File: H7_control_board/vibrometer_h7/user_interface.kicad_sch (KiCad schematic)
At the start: 14 parts, among them SW501 SW_Push

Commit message: working on getting ERC to run... almost there!
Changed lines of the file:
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@@
 					(size 1.27 1.27)
 				)
+				(hide yes)
 			)
 		)

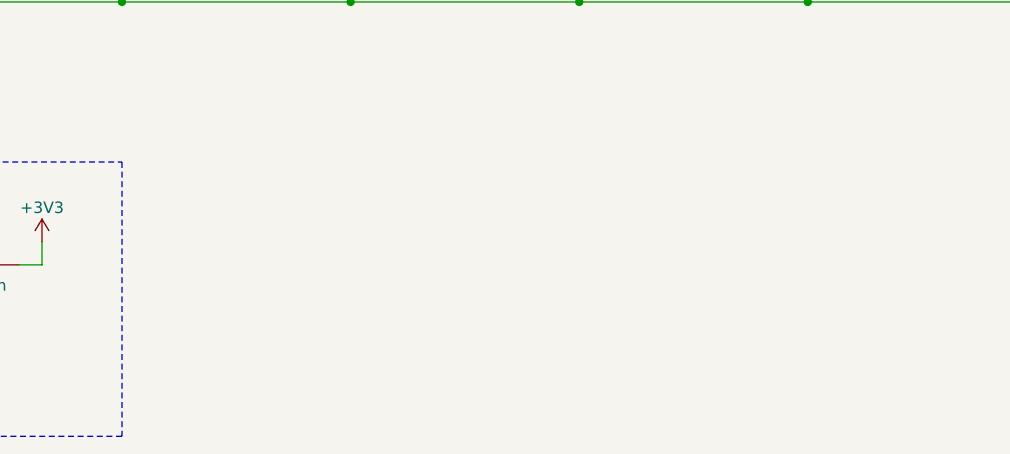
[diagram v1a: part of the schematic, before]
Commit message: adding strobe light to board itself
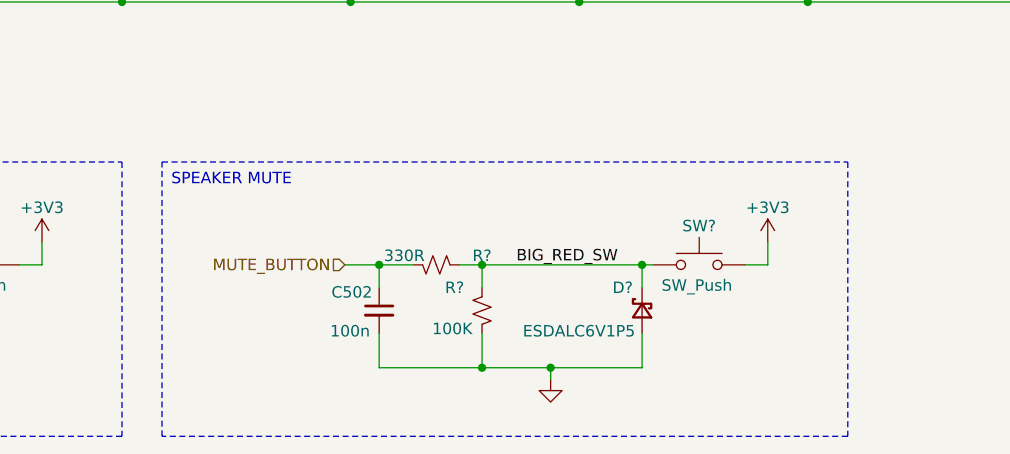
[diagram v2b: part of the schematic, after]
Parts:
- added C502: 100n, symbol Device:C_Small
- added D?: ESDALC6V1P5, symbol Device:D_Schottky_Small
- added R?: 100K, symbol Device:R_Small_US
- added R?: 330R, symbol Device:R_Small_US
- added SW?: SW_Push, symbol Switch:SW_Push
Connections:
- net +3V3: now also SW?.1
- net BIG_RED_SW: now also D?.1 (K), R?.1, R?.2, SW?.2
- net GND: now also C502.2, D?.2 (A), R?.1
- new net MUTE_BUTTON: C502.1, R?.2

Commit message: worked on audio output stuff, cleaned schematic
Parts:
- gave numbers to parts that had none: 3
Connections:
- net V_USB renamed +5V
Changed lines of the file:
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@@
+	)
+	(symbol
+		(lib_id "power:+5V")
+		(at 50.8 86.36 0)
+		(unit 1)
+		(exclude_from_sim no)
+		(in_bom yes)
+		(on_board yes)
+		(dnp no)
+		(property "Reference" "#PWR065"
+			(at 50.8 90.17 0)
+			(effects
+				(font
+					(size 1.27 1.27)
+				)
+				(hide yes)
+			)
+		)
+		(property "Value" "+5V"
+			(at 50.8 82.423 0)
+			(effects
+				(font
+					(size 1.27 1.27)
+				)
+			)
+		)
+		(property "Footprint" ""
+			(at 50.8 86.36 0)
+			(effects
+				(font
+					(size 1.27 1.27)
+				)
+				(hide yes)
+			)
+		)
+		(property "Datasheet" ""
+			(at 50.8 86.36 0)
+			(effects
+				(font
+					(size 1.27 1.27)
+				)
+				(hide yes)
+			)
+		)
+		(property "Description" "Power symbol creates a global label with name \"+5V\""
+			(at 50.8 86.36 0)
+			(effects
+				(font
+					(size 1.27 1.27)
+				)
+				(hide yes)
+			)
+		)
+		(pin "1"
+		)
+		(instances
+			(project "vibrometer_h7"
+				(path "/18de6987-156a-4b34-871e-cbbe1d261986/1264eea6-2da0-4b8c-9a4c-9121bcc9c76c"
+					(reference "#PWR065")
+					(unit 1)
+				)
+			)
+		)
 	)
 	(symbol
@@
 		(on_board yes)
 		(dnp no)
-		(property "Reference" "R?"
+		(property "Reference" "R504"
 			(at 163.957 140.97 0)
 			(effects
@@
 			(project "vibrometer_h7"
 				(path "/18de6987-156a-4b34-871e-cbbe1d261986/1264eea6-2da0-4b8c-9a4c-9121bcc9c76c"
-					(reference "R?")
-					(unit 1)
-				)
-			)
-		)
-	)
-	(symbol
-		(lib_id "power:+5V")
-		(at 50.8 86.36 0)
-		(unit 1)
-		(exclude_from_sim no)
-		(in_bom yes)
-		(on_board yes)
-		(dnp no)
-		(property "Reference" "#PWR065"
-			(at 50.8 90.17 0)
-			(effects
-				(font
-					(size 1.27 1.27)
-				)
-				(hide yes)
-			)
-		)
-		(property "Value" "V_USB"
-			(at 50.8 82.55 0)
-			(effects
-				(font
-					(size 1.27 1.27)
-				)
-			)
-		)
-		(property "Footprint" ""
-			(at 50.8 86.36 0)
-			(effects
-				(font
-					(size 1.27 1.27)
-				)
-				(hide yes)
-			)
-		)
-		(property "Datasheet" ""
-			(at 50.8 86.36 0)
-			(effects
-				(font
-					(size 1.27 1.27)
-				)
-				(hide yes)
-			)
-		)
-		(property "Description" "Power symbol creates a global label with name \"+5V\""
-			(at 50.8 86.36 0)
-			(effects
-				(font
-					(size 1.27 1.27)
-				)
-				(hide yes)
-			)
-		)
-		(pin "1"
-		)
-		(instances
-			(project "vibrometer_h7"
-				(path "/18de6987-156a-4b34-871e-cbbe1d261986/1264eea6-2da0-4b8c-9a4c-9121bcc9c76c"
-					(reference "#PWR065")
+					(reference "R504")
 					(unit 1)
 				)
@@
 		(on_board yes)
 		(dnp no)
-		(property "Reference" "D?"
+		(property "Reference" "D511"
 			(at 183.769 140.97 90)
 			(effects
@@
 			(project "vibrometer_h7"
 				(path "/18de6987-156a-4b34-871e-cbbe1d261986/1264eea6-2da0-4b8c-9a4c-9121bcc9c76c"
-					(reference "D?")
+					(reference "D511")
 					(unit 1)
 				)
@@
 		(on_board yes)
 		(dnp no)
-		(property "Reference" "R?"
+		(property "Reference" "R503"
 			(at 167.005 137.414 90)
 			(effects
@@
 			(project "vibrometer_h7"
 				(path "/18de6987-156a-4b34-871e-cbbe1d261986/1264eea6-2da0-4b8c-9a4c-9121bcc9c76c"
-					(reference "R?")
-					(unit 1)
-				)
+					(reference "R503")
+					(unit 1)
+				)

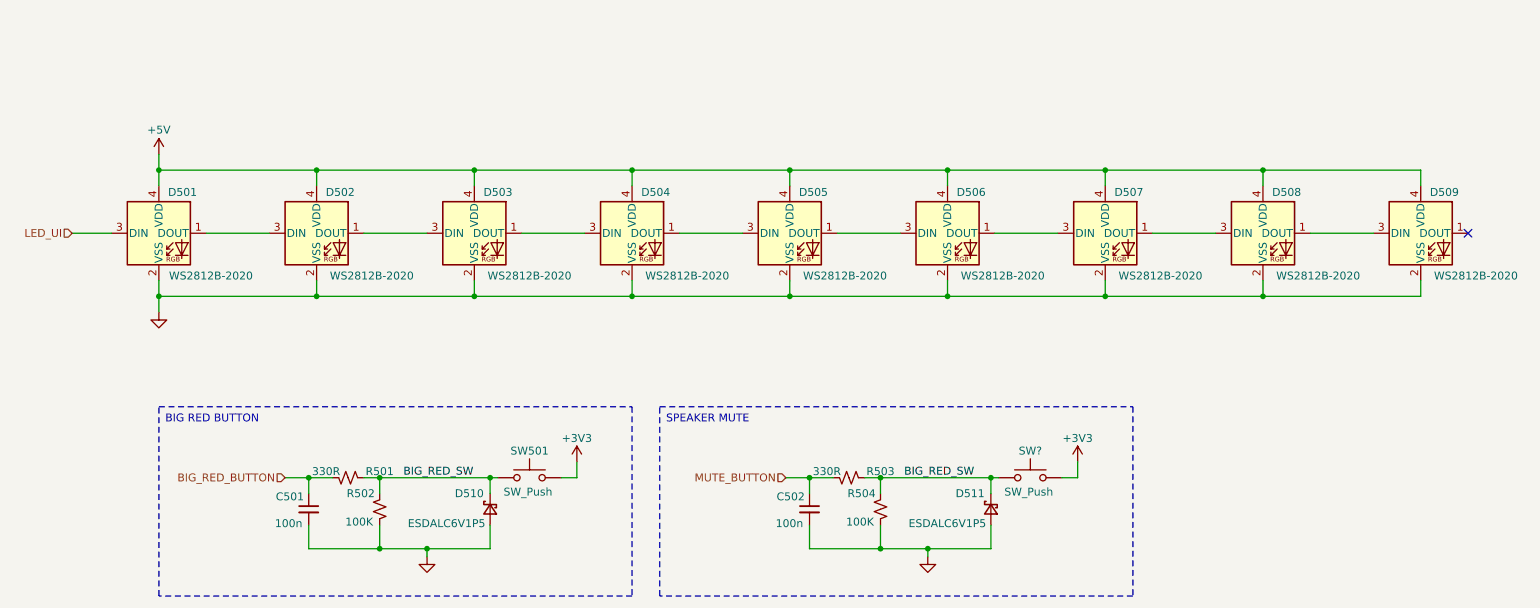
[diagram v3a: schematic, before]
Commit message: met with john to go over schematic. made changes, got rid of some leds...
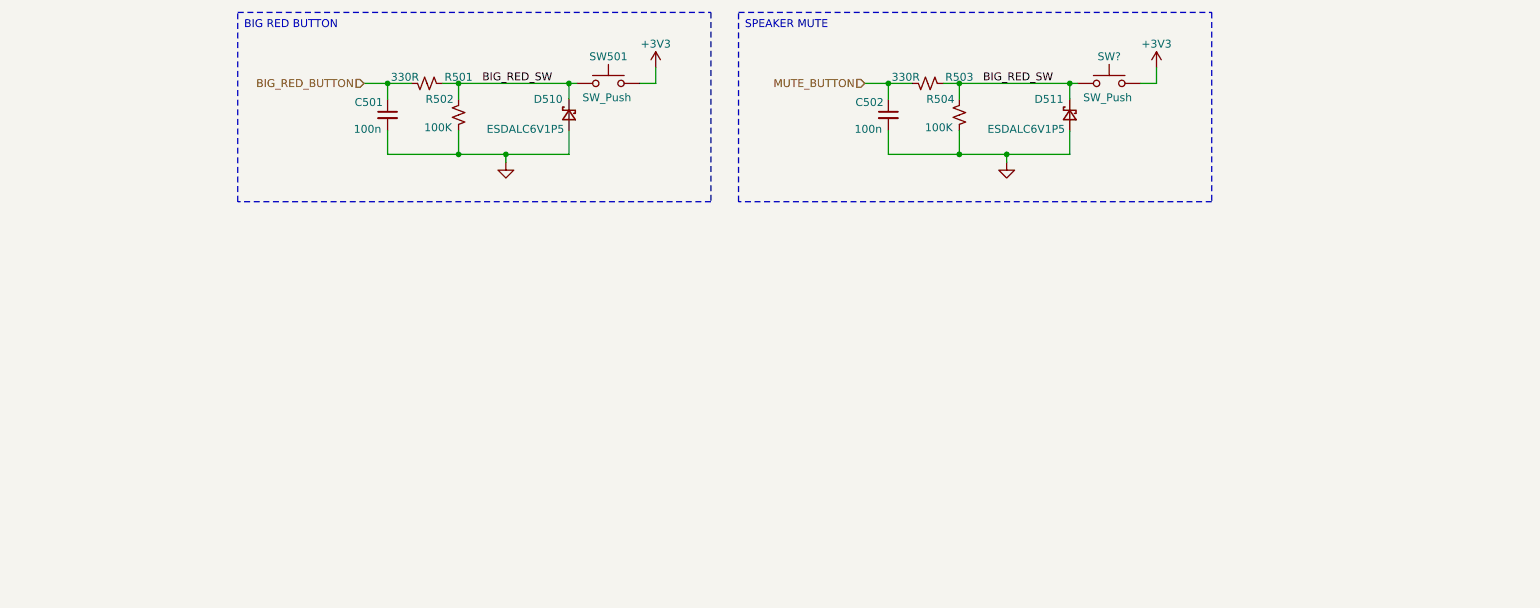
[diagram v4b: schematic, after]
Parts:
- removed D501, D502, D503, D504, D505, D506, D507, D508, D509: WS2812B-2020, LED_SMD:LED_WS2812B-2020_PLCC4_2.0x2.0mm, symbol LED:WS2812B-2020
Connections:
- no-connect marks 1 -> 0
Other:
- moved on the sheet: C501, C502, D510, D511, R501, R502, R503, R504, SW501, SW?

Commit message: started part selection
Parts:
- C501, C502: footprint (none) -> Capacitor_SMD:C_0603_1608Metric
- SW501, SW?: footprint (none) -> Button_Switch_SMD:SW_Push_1P1T_XKB_TS-1187A; LCSC (none) -> C318884
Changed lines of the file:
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@@
 			)
 		)
-		(property "Footprint" ""
+		(property "Footprint" "Capacitor_SMD:C_0603_1608Metric"
 			(at 168.275 80.01 0)
 			(effects
@@
 			)
 		)
-		(property "Footprint" ""
+		(property "Footprint" "Button_Switch_SMD:SW_Push_1P1T_XKB_TS-1187A"
 			(at 203.835 69.85 0)
 			(effects
@@
 			)
 		)
-		(property "Datasheet" "~"
+		(property "Datasheet" "https://www.lcsc.com/datasheet/lcsc_datasheet_2304140030_XKB-Connection-TS-1187A-B-A-B_C318884.pdf"
 			(at 203.835 69.85 0)
 			(effects
@@
 			)
 		)
-		(property "LCSC" ""
+		(property "LCSC" "C318884"
 			(at 203.835 74.93 0)
 			(effects
@@
 			)
 		)
-		(property "Footprint" ""
+		(property "Footprint" "Button_Switch_SMD:SW_Push_1P1T_XKB_TS-1187A"
 			(at 123.19 69.85 0)
 			(effects
@@
 			)
 		)
-		(property "Datasheet" "~"
+		(property "Datasheet" "https://www.lcsc.com/datasheet/lcsc_datasheet_2304140030_XKB-Connection-TS-1187A-B-A-B_C318884.pdf"
 			(at 123.19 69.85 0)
 			(effects
@@
 			)
 		)
-		(property "LCSC" ""
+		(property "LCSC" "C318884"
 			(at 123.19 74.93 0)
 			(effects
@@
 			)
 		)
-		(property "Footprint" ""
+		(property "Footprint" "Capacitor_SMD:C_0603_1608Metric"
 			(at 87.63 80.01 0)
 			(effects

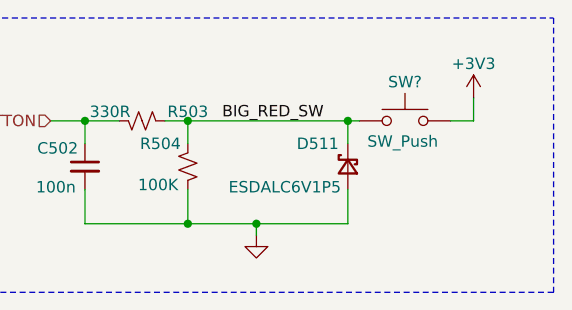
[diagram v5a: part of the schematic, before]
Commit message: component selection, headphone amp circuit specs
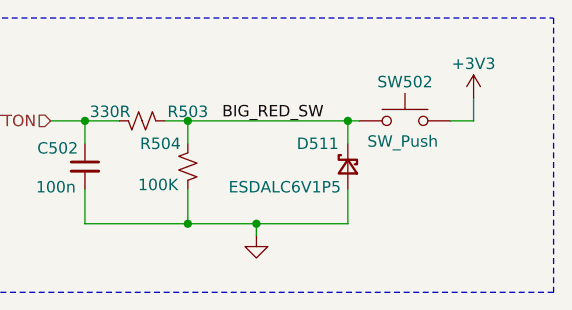
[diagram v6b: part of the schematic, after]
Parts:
- C501, C502: footprint Capacitor_SMD:C_0603_1608Metric -> Capacitor_SMD:C_0402_1005Metric_Pad0.74x0.62mm_HandSolder; LCSC (none) -> C307331
- gave numbers to parts that had none: 1
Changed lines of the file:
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@@
 			)
 		)
-		(property "Footprint" "Capacitor_SMD:C_0603_1608Metric"
+		(property "Footprint" "Capacitor_SMD:C_0402_1005Metric_Pad0.74x0.62mm_HandSolder"
 			(at 168.275 80.01 0)
 			(effects
@@
 			)
 		)
-		(property "Datasheet" "~"
+		(property "Datasheet" "https://wmsc.lcsc.com/wmsc/upload/file/pdf/v2/lcsc/2304140030_Samsung-Electro-Mechanics-CL05B104KB54PNC_C307331.pdf"
 			(at 168.275 80.01 0)
 			(effects
@@
 			)
 		)
-		(property "LCSC" ""
+		(property "LCSC" "C307331"
 			(at 168.275 80.01 0)
 			(effects
@@
 		(on_board yes)
 		(dnp no)
-		(property "Reference" "SW?"
+		(property "Reference" "SW502"
 			(at 203.835 70.612 0)
 			(effects
@@
 			(project "vibrometer_h7"
 				(path "/18de6987-156a-4b34-871e-cbbe1d261986/1264eea6-2da0-4b8c-9a4c-9121bcc9c76c"
-					(reference "SW?")
+					(reference "SW502")
 					(unit 1)
 				)
@@
 			)
 		)
-		(property "Footprint" "Capacitor_SMD:C_0603_1608Metric"
+		(property "Footprint" "Capacitor_SMD:C_0402_1005Metric_Pad0.74x0.62mm_HandSolder"
 			(at 87.63 80.01 0)
 			(effects
@@
 			)
 		)
-		(property "Datasheet" "~"
+		(property "Datasheet" "https://wmsc.lcsc.com/wmsc/upload/file/pdf/v2/lcsc/2304140030_Samsung-Electro-Mechanics-CL05B104KB54PNC_C307331.pdf"
 			(at 87.63 80.01 0)
 			(effects
@@
 			)
 		)
-		(property "LCSC" ""
+		(property "LCSC" "C307331"
 			(at 87.63 80.01 0)
 			(effects

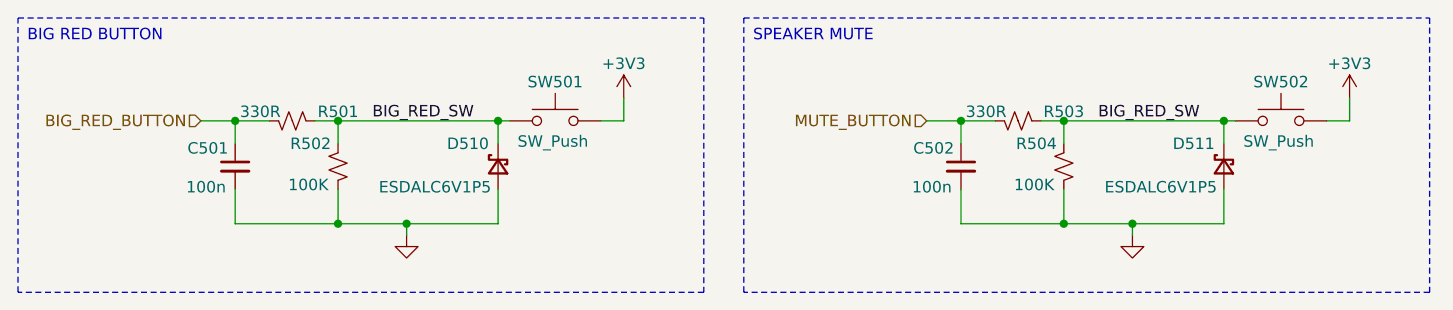
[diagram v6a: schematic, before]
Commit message: part selection for audio, schematic cleanup
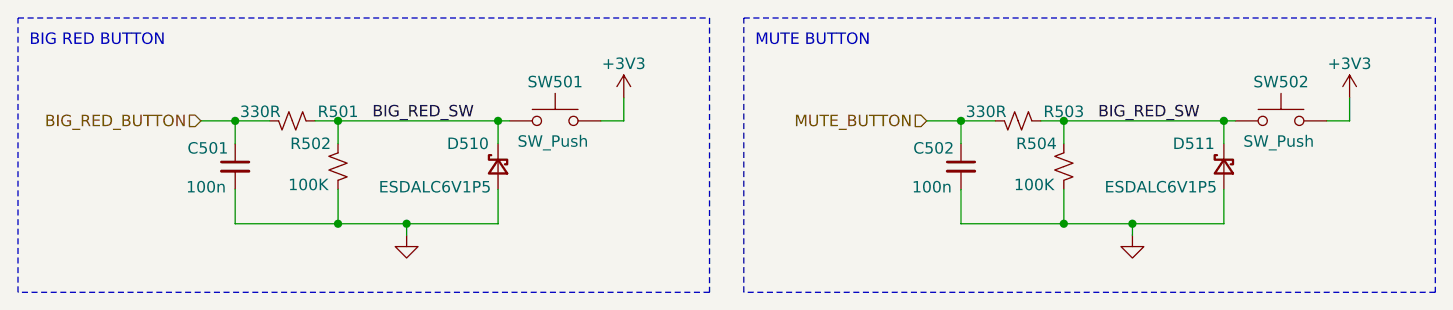
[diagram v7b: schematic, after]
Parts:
- D510: footprint (none) -> Package_TO_SOT_SMD:Diodes_SOT-553
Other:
- note added: "BIG RED BUTTON"
- note added: "MUTE BUTTON"
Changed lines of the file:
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@@
 		)
 	)
-	(text_box "BIG RED BUTTON"
-		(exclude_from_sim no)
-		(at 63.5 63.5 0)
-		(size 76.2 30.48)
+	(rectangle
+		(start 144.145 63.5)
+		(end 220.98 93.98)
 		(stroke
 			(width 0)
@@
 			(type none)
 		)
-		(effects
-			(font
-				(size 1.27 1.27)
-			)
-			(justify left top)
-		)
 	)
-	(text_box "SPEAKER MUTE"
-		(exclude_from_sim no)
-		(at 144.145 63.5 0)
-		(size 76.2 30.48)
+	(rectangle
+		(start 63.5 63.5)
+		(end 140.335 93.98)
 		(stroke
 			(width 0)
@@
 			(type none)
 		)
+	)
+	(text "BIG RED BUTTON"
+		(exclude_from_sim no)
+		(at 64.77 66.04 0)
 		(effects
 			(font
 				(size 1.27 1.27)
 			)
-			(justify left top)
+			(justify left)
+		)
+	)
+	(text "MUTE BUTTON"
+		(exclude_from_sim no)
+		(at 145.415 66.04 0)
+		(effects
+			(font
+				(size 1.27 1.27)
+			)
+			(justify left)
 		)
 	)
@@
 			)
 		)
-		(property "Footprint" ""
+		(property "Footprint" "Package_TO_SOT_SMD:Diodes_SOT-553"
 			(at 116.84 80.01 90)
 			(effects

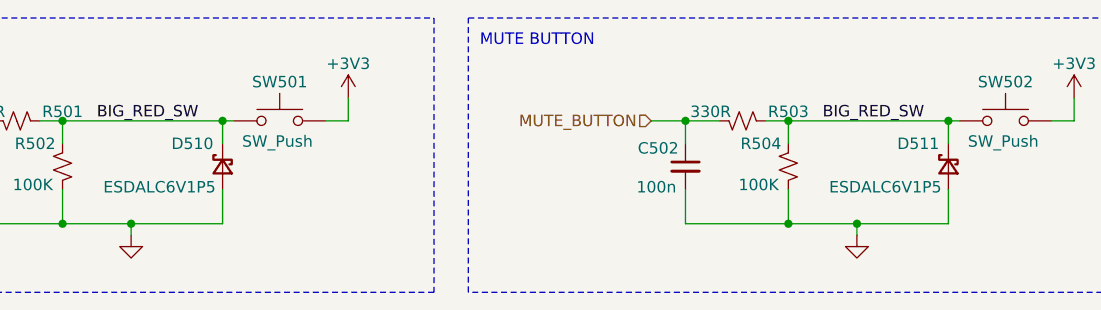
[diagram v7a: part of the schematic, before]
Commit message: updated reference designator naming
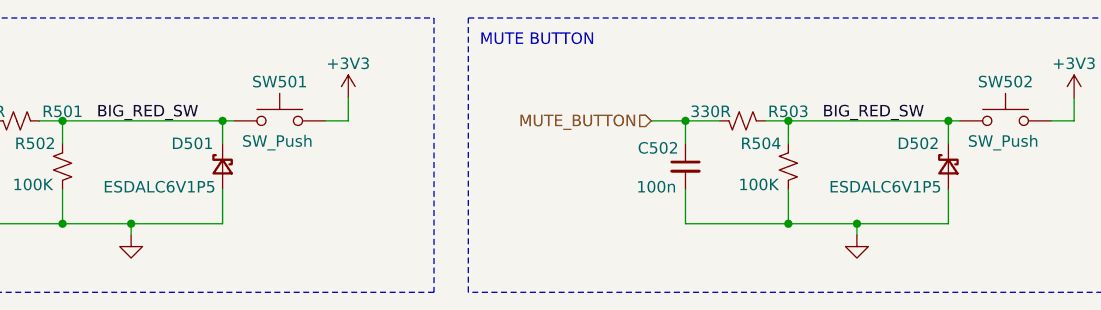
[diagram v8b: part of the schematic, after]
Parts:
- renumbered D510 to D501, D511 to D502
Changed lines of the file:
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@@
 		(on_board yes)
 		(dnp no)
-		(property "Reference" "#PWR061"
+		(property "Reference" "#PWR0504"
 			(at 211.455 76.2 0)
 			(effects
@@
 			(project "vibrometer_h7"
 				(path "/18de6987-156a-4b34-871e-cbbe1d261986/1264eea6-2da0-4b8c-9a4c-9121bcc9c76c"
-					(reference "#PWR061")
+					(reference "#PWR0504")
 					(unit 1)
 				)
@@
 		(on_board yes)
 		(dnp no)
-		(property "Reference" "D510"
+		(property "Reference" "D501"
 			(at 115.824 77.47 90)
 			(effects
@@
 			(project "vibrometer_h7"
 				(path "/18de6987-156a-4b34-871e-cbbe1d261986/1264eea6-2da0-4b8c-9a4c-9121bcc9c76c"
-					(reference "D510")
+					(reference "D501")
 					(unit 1)
 				)
@@
 		(on_board yes)
 		(dnp no)
-		(property "Reference" "#PWR016"
+		(property "Reference" "#PWR0502"
 			(at 130.81 76.2 0)
 			(effects
@@
 			(project "vibrometer_h7"
 				(path "/18de6987-156a-4b34-871e-cbbe1d261986/1264eea6-2da0-4b8c-9a4c-9121bcc9c76c"
-					(reference "#PWR016")
+					(reference "#PWR0502")
 					(unit 1)
 				)
@@
 		(on_board yes)
 		(dnp no)
-		(property "Reference" "#PWR017"
+		(property "Reference" "#PWR0501"
 			(at 106.68 93.98 0)
 			(effects
@@
 			(project "vibrometer_h7"
 				(path "/18de6987-156a-4b34-871e-cbbe1d261986/1264eea6-2da0-4b8c-9a4c-9121bcc9c76c"
-					(reference "#PWR017")
+					(reference "#PWR0501")
 					(unit 1)
 				)
@@
 		(on_board yes)
 		(dnp no)
-		(property "Reference" "D511"
+		(property "Reference" "D502"
 			(at 196.469 77.47 90)
 			(effects
@@
 			(project "vibrometer_h7"
 				(path "/18de6987-156a-4b34-871e-cbbe1d261986/1264eea6-2da0-4b8c-9a4c-9121bcc9c76c"
-					(reference "D511")
+					(reference "D502")
 					(unit 1)
 				)
@@
 		(on_board yes)
 		(dnp no)
-		(property "Reference" "#PWR060"
+		(property "Reference" "#PWR0503"
 			(at 187.325 93.98 0)
 			(effects
@@
 			(project "vibrometer_h7"
 				(path "/18de6987-156a-4b34-871e-cbbe1d261986/1264eea6-2da0-4b8c-9a4c-9121bcc9c76c"
-					(reference "#PWR060")
-					(unit 1)
-				)
+					(reference "#PWR0503")
+					(unit 1)
+				)
